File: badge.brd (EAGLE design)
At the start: 53.8 x 85.3 mm, 33 parts, among them IC1 MCP1703CB, U1 ESP8266, U2 AT25SF041-SOIC8, Y1 26MHz

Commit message: for ys
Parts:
- removed D2: 1N4148, adafruit:SOD-323F
- removed E1: ANTENNATRACE, SparkFun-RF:TRACE_ANTENNA_2.4GHZ_25.7MM
- removed IC1: MCP1703CB, linear:SOT23
- removed JP2: (no value), pinhead:1X05
- removed JP3: (no value), pinhead:1X04
- removed S1, S2, S3, S4, S5: (no value), gm2:TACT-SW-4P-SMD
- removed Y1: 26MHz, SparkFun-FreqCtrl:CRYSTAL-SMD-5X3
- added ANT1: AN9520, badge:AN9520
- added D3: 1N4148, adafruit:SOD-323F
- added SW1: MK12C02, badge:MK12C02
- added U$1, U$2, U$3, U$4, U$5, U$6: TOUCHSWITCH, badge:EVQQWN03W
- added U3: LM317EMP-SOT223, Seeed-OPL-ic:SOT-223
- added XTAL1: 26MHZ, badge:XRCGB_F_P
- C1, C2, C3, C4, C5, C6, C7, C8, C9: device rcl:C0805 -> resistor:C0603K
- R1, R2, R3, R4, R5, R6: device rcl:R0805 -> resistor:R0603W
- moved C3 64.4 mm to (74.9, 26.4), turned to 0 degrees
- moved C2 58.7 mm to (80.2, 37.9), turned to 90 degrees
- moved R1 55.9 mm to (82.4, 37.1)
- moved R2 55.1 mm to (72.7, 40.2), turned to 0 degrees
- moved U1 52.0 mm to (74.9, 35.6)
- moved C6 50.6 mm to (82.4, 34.3), turned to 180 degrees
- moved R6 50.3 mm to (68.3, 31.4), turned to 270 degrees
- moved U2 49.7 mm to (74.9, 29.7), turned to 90 degrees
- moved C8 48.8 mm to (79.1, 41.1), turned to 270 degrees
- moved D1 48.3 mm to (70.0, 31.4), turned to 270 degrees
- moved R4 45.9 mm to (77.8, 41.1), turned to 90 degrees
- moved C7 44.3 mm to (82.4, 35.7)
- moved JP1 42.0 mm to (87.6, 33.5), turned to 90 degrees
- moved C1 41.9 mm to (74.9, 41.1)
- moved C4 35.6 mm to (22.2, 40.8), turned to 180 degrees
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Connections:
- removed net GPIO2: JP3.2, S1.1, S1.2, U1.14
- removed net N$7: C7.1, U1.28, Y1.1
- removed net SPI_CLK: JP2.4, LCD1.2, U1.9
- removed net SPI_CS: JP2.5, S4.1, S4.2, U1.13
- removed net SPI_SI: JP2.3, LCD1.3, U1.12
- removed net SPI_SO: JP2.2, LCD1.4, U1.10
- new net ANT: ANT1.P$1, U1.2
- new net GPIO12/SPI_SO: LCD1.4, U1.10
- new net GPIO13/SPI_SI: LCD1.3, U1.12
- new net GPIO14/SPI_CLK/SCL: LCD1.2, U1.9
- new net GPIO15/SPI_CS: U$3.P$2, U$3.P$3, U$4.P$2, U$4.P$3, U1.13
- new net GPIO16: U1.8
- new net GPIO2/SDA: U$1.P$1, U$1.P$4, U$3.P$1, U$3.P$4, U$5.P$1, U$5.P$4, U1.14
- net 5V: now also D3.A
- net ADC: no longer JP2.1
- net GND: now also C6.1, C7.1, U3.1; no longer C6.2, C7.2, E1.GND, E1.GND2, IC1.1, S1.3, S1.4, S2.3, S2.4, S3.3, S3.4, S4.3, S4.4, S5.3, S5.4
- net GPIO0: now also U$5.P$2, U$5.P$3, U$6.P$2, U$6.P$3; no longer JP3.1, S5.1, S5.2
- net GPIO4: now also U$2.P$1, U$2.P$4, U$4.P$1, U$4.P$4, U$6.P$1, U$6.P$4; no longer JP3.3, S2.1, S2.2
- net GPIO5: now also U$1.P$2, U$1.P$3, U$2.P$2, U$2.P$3; no longer JP3.4, S3.1, S3.2
- net N$1: now also SW1.P$2, U3.3; no longer E1.ANT, U1.2
- net N$5: now also D3.C, SW1.P$1; no longer IC1.3
- net N$6: now also C6.2, U1.27, XTAL1.P$2; no longer D2.C, U1.8
- net N$8: now also C7.2, U1.28, XTAL1.P$4; no longer C6.1, U1.27, Y1.3
- net RESET: no longer D2.A
- net VCC: now also U3.2, U3.TER; no longer IC1.2
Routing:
- net GND: track 60.7 -> 0.00 mm
- net GPIO4: track 0.00 -> 20.4 mm
- net GPIO2/SDA: track 0.00 -> 20.4 mm
- net GPIO15/SPI_CS: track 0.00 -> 13.6 mm
- net ANT: track 0.00 -> 7.69 mm
- net GPIO5: track 0.00 -> 7.41 mm
- net GPIO0: track 9.10 -> 13.6 mm
- removed copper zone on layer 1, net GND
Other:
- board size 53.8 x 85.3 mm -> 90 x 50 mm

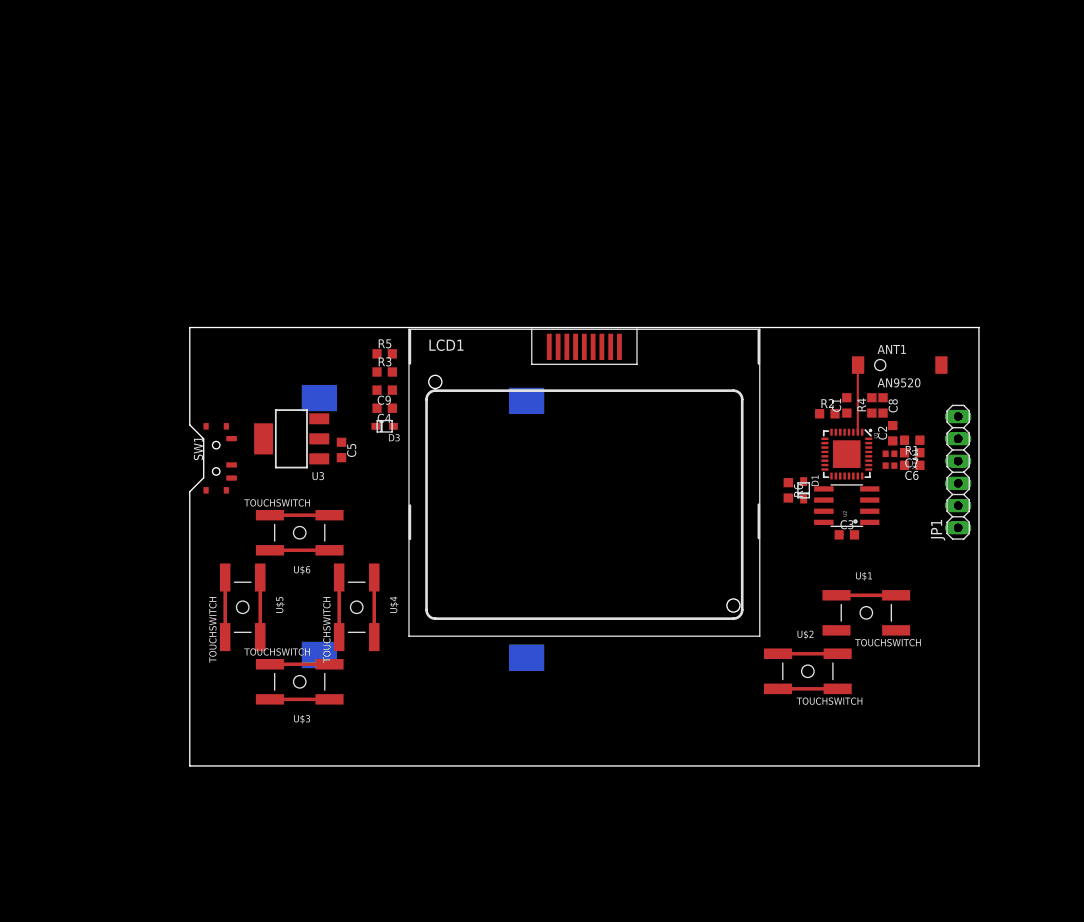
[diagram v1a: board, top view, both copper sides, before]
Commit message: switching over to ESP-12e/f
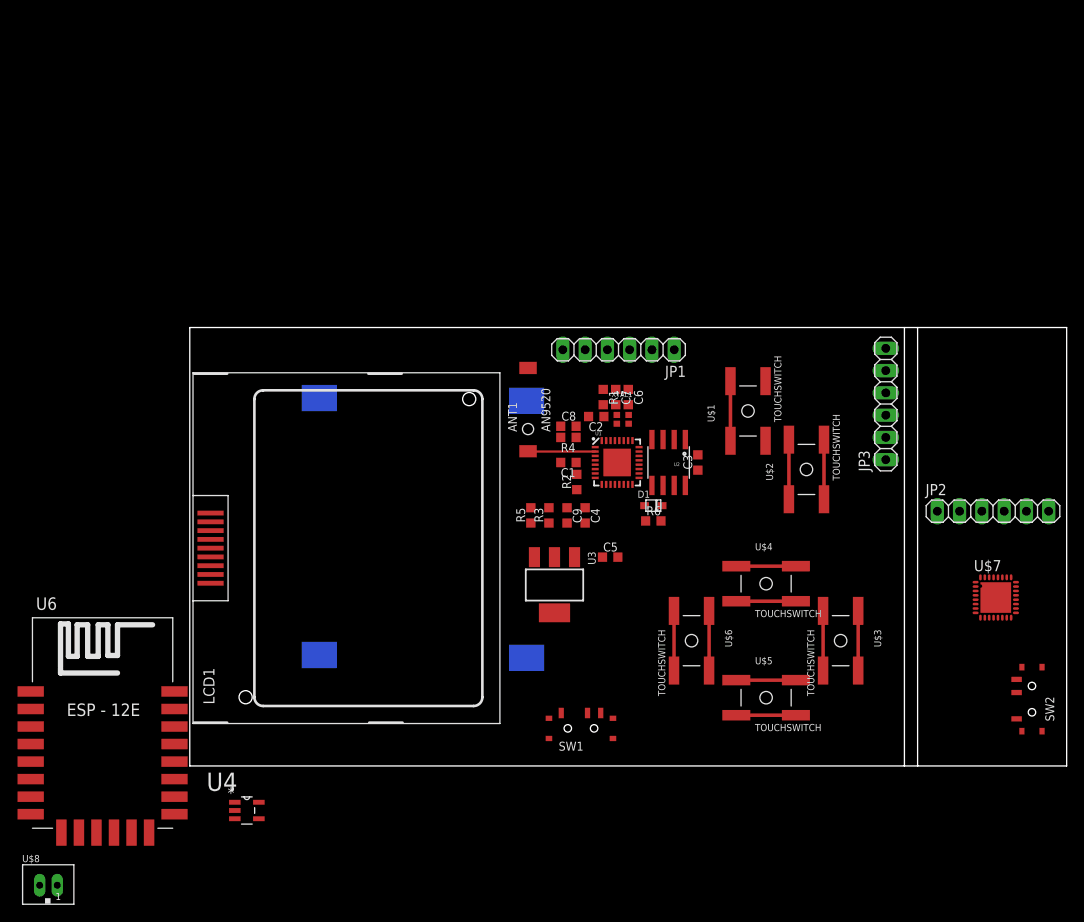
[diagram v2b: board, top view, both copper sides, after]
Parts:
- removed D3: 1N4148, adafruit:SOD-323F
- added JP2, JP3: (no value), pinhead:1X06
- added SW2: MK12C02, badge:MK12C02
- added U$7: CY7C65213-32LTXI, cypress_usb-serial:QFN32
- added U$8: JST-PH_2-PIN_HEADER, SRG:JST_B2B-PH_HEADER
- added U4: MCP73832T-2DCI/OT, Microchip_By_element14_Batch_1:SOT95P300X145-5N
- added U6: (no value), esp8266modules:ESP12E-SMD
- moved U$3 61.9 mm to (74.2, 14.3), turned to 180 degrees
- moved U$5 60.6 mm to (65.7, 7.79), turned to 270 degrees
- moved SW1 51.8 mm to (44.6, 4.29), turned to 0 degrees
- moved U$4 46.8 mm to (65.7, 20.8), turned to 270 degrees
- moved U$6 46.3 mm to (57.2, 14.3), turned to 180 degrees
- moved ANT1 42.7 mm to (38.6, 40.6), turned to 90 degrees
- moved JP1 41.2 mm to (48.9, 47.5), turned to 180 degrees
- moved C8 36.0 mm to (43.2, 38.7), turned to 0 degrees
- moved R1 35.6 mm to (47.1, 42.1), turned to 270 degrees
- moved R4 34.8 mm to (43.2, 37.5), turned to 180 degrees
- moved C7 34.4 mm to (48.6, 42.1), turned to 270 degrees
- moved U3 34.3 mm to (41.6, 20.6), turned to 180 degrees
- moved C2 33.9 mm to (46.4, 39.8), turned to 180 degrees
- moved C6 33.3 mm to (50.0, 42.1), turned to 270 degrees
- moved C5 33.0 mm to (47.9, 23.8), turned to 0 degrees
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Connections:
- new net AGND: U$7.24
- new net N$10: JP2.2, JP3.2
- new net N$11: JP2.3, JP3.3
- new net N$12: JP2.4, JP3.4
- new net N$13: JP2.5, JP3.5
- new net N$14: JP2.6, JP3.6
- new net N$7: JP2.1, JP3.1
- new net VCCD: U$7.16
- new net VCCIO: U$7.1
- new net VDD: U4.4
- net 5V: now also SW1.P$3; no longer D3.A
- net GND: now also U$7.17, U$7.20, U$7.4
- net N$1: now also C4.1, SW1.P$1; no longer SW1.P$2
- net N$5: now also SW1.P$2; no longer C4.1, D3.C, SW1.P$1
- net VCC: now also U$7.19
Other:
- board size 90 x 50 mm -> 100 x 50 mm

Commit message: before the big change
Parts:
- removed ANT1: AN9520, badge:AN9520
- removed B1, B2: BATTERY, gm2:BATT-HOLDER-20MM
- removed D1: 1N4148, adafruit:SOD-323F
- removed JP1, JP2, JP3: (no value), pinhead:1X06
- removed SW2: MK12C02, badge:MK12C02
- removed U$6: TOUCHSWITCH, badge:EVQQWN03W
- removed U$8: JST-PH_2-PIN_HEADER, SRG:JST_B2B-PH_HEADER
- removed U1: ESP8266, SparkFun-RF:QFN32
- removed U2: AT25SF041-SOIC8, SparkFun-RF:SO08
- removed U3: LM317EMP-SOT223, Seeed-OPL-ic:SOT-223
- removed XTAL1: 26MHZ, badge:XRCGB_F_P
- added C10, C12: 0.1uF, resistor:C0603K
- added C11: 4.7uF, resistor:C0603K
- added CON1: PH_2, badge:PH_2
- added J1, J2: (no value), SparkFun-Connectors:1X03
- added J10: (no value), SparkFun-Connectors:1X14
- added J3, J4: (no value), SparkFun-Connectors:1X06
- added J5, J6, J8: (no value), SparkFun-Connectors:1X10
- added LED1, LED2, LED3: (no value), led:SML0805
- added R10, R7, R8, R9: 470, resistor:R0603W
- added R11: 590k, resistor:R0603W
- added R12: 280k, resistor:R0603W
- added R13: 82k, resistor:R0603W
- added R14, R15: 1k, resistor:R0603W
- added SJ1, SJ2, SJ3, SJ4: SOLDERJUMPERTRACE, SparkFun-Retired:SJ_2S-TRACE
- added U$10: USBMICRO, badge:USBMICRO
- added U$11: MCP1824T-ADJE/OT, Microchip_By_element14_Batch_1:SOT95P270X145-5N
- added U$9: MCP1824T-3302E/OT, Microchip_By_element14_Batch_1:SOT95P270X145-5N
- C1: value 10uF -> 4.7uF
- C2, C3: value 0.1uF -> 4.7uF
- C4: value 1uF -> 1uF/X7R
- C5: value 10uF -> 1uF/X7R
- C6: value 12pF -> 1uF
- C7: value 12pF -> 1uF/X7R
- C8: value 1uF -> 4.7uF
- R1: value 12k -> 100k
- R2: value 12K -> 470
- R4: value 12K -> 100k
- R6: value 12K -> 2k
- moved U6 72.2 mm to (54.6, 35.2), turned to 90 degrees
- moved R1 56.3 mm to (92.0, 8.10), turned to 0 degrees
- moved C6 50.2 mm to (91.4, 13.7), turned to 180 degrees
- moved C7 49.8 mm to (93.0, 19.7), turned to 90 degrees
- moved C8 47.0 mm to (89.9, 33.5)
- moved C9 44.3 mm to (3.41, 8.65), turned to 90 degrees
- moved U4 43.5 mm to (45.9, 13.4), turned to 90 degrees
- moved C3 40.6 mm to (90.9, 11.0)
- moved R3 39.8 mm to (3.41, 15.5)
- moved R5 39.1 mm to (3.41, 12.1), turned to 270 degrees
- moved C2 31.6 mm to (49.5, 8.41)
- moved U$5 30.4 mm to (73.7, 37.1), turned to 180 degrees
- moved U$1 27.8 mm to (54.5, 14.3)
- moved C1 24.5 mm to (43.3, 10.1), turned to 90 degrees
- moved R2 22.4 mm to (41.8, 10.1)
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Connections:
- removed net AGND: U$7.24
- removed net ANT: ANT1.P$1, U1.2
- removed net N$13: JP2.5, JP3.5
- removed net N$14: JP2.6, JP3.6
- removed net N$15: JP1.5
- removed net N$2: R1.2, U1.31
- removed net N$5: B1.+, SW1.P$2
- removed net N$8: C7.2, U1.28, XTAL1.P$4
- removed net SD_CLK: U1.21, U2.6
- removed net SD_CS0: U1.20, U2.1
- removed net SD_HD: U1.18, U2.7
- removed net SD_SI: U1.23, U2.5
- removed net SD_SO: U1.22, U2.2
- removed net SD_WP: U1.19, U2.3
- removed net U0RX: JP1.3, U1.25
- removed net U0TX: JP1.2, U1.26
- removed net VCCD: U$7.16
- removed net VCCIO: U$7.1
- removed net VDD: U4.4
- new net BATT+: C1.1, CON1.P$2, SW1.P$3, U4.3
- new net CH_PD: J8.6, SJ1.2, U6.CH_PD
- new net CS0: J10.1, U6.CS0
- new net CTS: J5.8, U$7.8
- new net D+: U$10.P$D+, U$7.14
- new net D-: U$10.P$D-, U$7.15
- new net DCD: J5.4, U$7.7
- new net DSR: J5.5, U$7.6
- new net GPIO10: J10.5, U6.GPIO10
- new net GPIO9: J10.6, U6.GPIO9
- new net ID: U$10.P$ID
- new net MISO: J10.2, U6.MISO
- new net MOSI: J10.3, U6.MOSI
- new net N$16: J1.1, R11.2
- new net N$17: J1.3, R12.2
- new net N$18: R10.2, R9.1, U$7.18
- new net N$19: C6.1, J1.2, J2.1, U$11.5
- new net N$20: C7.2, U$7.16
- new net N$28: R14.1, SJ3.2
- new net N$30: R15.1, SJ4.2
- new net RI: J5.3, U$7.3
- new net RTS: J3.5, J4.5, J5.7, SJ2.1, U$7.32
- new net RX: J10.13, J3.3, J4.3, J5.10, U$7.30, U6.RXD0
- new net SCLK: J10.4, U6.SCLK
- new net TX: J10.14, J3.2, J4.2, J5.9, U$7.2, U6.TXD0
- new net USB_GPIO0: J6.3, U$7.22
- new net USB_GPIO1: J6.4, U$7.21
- new net USB_GPIO2: J6.5, U$7.10
- new net USB_GPIO3: J6.6, U$7.11
- new net USB_GPIO4: J6.7, U$7.9
- new net USB_GPIO5: J6.8, U$7.5
- new net USB_GPIO6: J6.9, U$7.12
- new net USB_GPIO7: J6.10, U$7.13
- new net VADJ: R11.1, R12.1, R13.2, U$11.4
- new net V_IO: C11.2, C12.2, J2.2, J6.1, U$7.1
- net 5V: now also C10.2, C2.1, C3.2, C8.2, J2.3, J3.4, J4.4, J5.1, LED1.A, LED3.A, R9.2, SW1.P$2, U$10.P$VCC, U$11.1, U$7.19, U4.4; no longer JP1.4, SW1.P$3
- net ADC: now also J8.7, U6.ADC; no longer U1.6
- net DTR: now also J3.1, J4.1, J5.6, SJ1.1, U$7.31; no longer C8.1, D1.C, JP1.1
- net GND: now also C10.1, C11.1, C12.1, C3.1, C6.2, C8.1, CON1.P$1, J10.11, J10.12, J3.6, J4.6, J5.2, J6.2, J8.8, R10.1, R13.1, R14.2, R4.1, R6.1, R7.1, R8.1, U$10.P$GND, U$11.2, U$7.24, U$9.2, U4.2, U6.GND; no longer B2.-, C3.2, C6.1, JP1.6, U1.EP, U2.4, U3.1
- net GPIO0: now also J10.10, SJ4.1, U6.GPIO0; no longer D1.A, R6.1, U$5.P$2, U$5.P$3, U$6.P$2, U$6.P$3, U1.15
- net GPIO12/SPI_SO: now also J8.5, U6.GPIO12; no longer U1.10
- net GPIO13/SPI_SI: now also J8.4, U6.GPIO13; no longer U1.12
- net GPIO14/SPI_CLK/SCL: now also J8.3, U6.GPIO14; no longer U1.9
- net GPIO15/SPI_CS: now also J8.2, SJ3.1, U6.GPIO15; no longer U$3.P$2, U$3.P$3, U$4.P$2, U$4.P$3, U1.13
- net GPIO16: now also J8.1, U6.GPIO16; no longer U1.8
- net GPIO2/SDA: now also J10.9, U6.GPIO2; no longer U$1.P$1, U$1.P$4, U$3.P$1, U$3.P$4, U$5.P$1, U$5.P$4, U1.14
- net GPIO4: now also J10.8, U6.GPIO4; no longer U$2.P$1, U$2.P$4, U$4.P$1, U$4.P$4, U$6.P$1, U$6.P$4, U1.16
- net GPIO5: now also J10.7, U6.GPIO5; no longer U$1.P$2, U$1.P$3, U$2.P$2, U$2.P$3, U1.24
- net N$1: now also U$9.1; no longer U3.3
- net N$10: now also R2.1, U4.1; no longer JP2.2, JP3.2
- net N$11: now also R1.2, U$11.3; no longer JP2.3, JP3.3
- net N$12: now also LED3.C, R8.2; no longer JP2.4, JP3.4
- net N$4: now also R4.2, U$9.3; no longer R2.1, U1.7
- net N$6: now also R6.2, U4.5; no longer C6.2, U1.27, XTAL1.P$2
- net N$7: now also LED2.C, R7.2; no longer JP2.1, JP3.1
- net N$9: now also LED1.C, R2.2; no longer B1.-, B2.+
- net RESET: now also SJ2.2, U6.RESET; no longer C8.2, R4.1, U1.32
- net VCC: now also J8.10, J8.9, LED2.A, R15.2, U$9.5, U6.VCC; no longer C1.1, C2.1, C3.1, R2.2, R4.2, R6.2, U$7.19, U1.1, U1.11, U1.17, U1.29, U1.3, U1.30, U1.4, U2.8, U3.2, U3.TER
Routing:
- net GND: track 0.00 -> 227.7 mm, vias 0 -> 8
- net 5V: track 0.00 -> 182.0 mm, vias 0 -> 4
- net VCC: track 0.00 -> 112.0 mm, vias 0 -> 2
- net GPIO12/SPI_SO: track 0.00 -> 104.7 mm, vias 0 -> 3
- net GPIO13/SPI_SI: track 0.00 -> 104.5 mm, vias 0 -> 3
- net GPIO14/SPI_CLK/SCL: track 0.00 -> 104.4 mm, vias 0 -> 1
- net RX: track 0.00 -> 62.7 mm, vias 0 -> 2
- net TX: track 0.00 -> 57.2 mm
- net ADC: track 0.00 -> 55.7 mm, vias 0 -> 1
- net CH_PD: track 0.00 -> 53.5 mm, vias 0 -> 1
- net GPIO16: track 0.00 -> 51.9 mm, vias 0 -> 2
- net GPIO15/SPI_CS: track 13.6 -> 56.6 mm, vias 0 -> 1
- net RTS: track 0.00 -> 30.6 mm
- net DTR: track 0.00 -> 29.4 mm, vias 0 -> 1
- net CS0: track 0.00 -> 24.7 mm, vias 0 -> 1
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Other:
- outline, holes or cut-outs redrawn
- board text added: "Init:6.25mil"

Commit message: the change cometh
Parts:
- removed C10, C12: 0.1uF, resistor:C0603K
- removed C11, C8: 4.7uF, resistor:C0603K
- removed C6: 1uF, resistor:C0603K
- removed C7: 1uF/X7R, resistor:C0603K
- removed J4: (no value), SparkFun-Connectors:1X06
- removed J5, J6: (no value), SparkFun-Connectors:1X10
- removed U$11: MCP1824T-ADJE/OT, Microchip_By_element14_Batch_1:SOT95P270X145-5N
- removed U$7: CY7C65213-32LTXI, cypress_usb-serial:QFN32
- added IC1: CP2102, silabs:MLP28
- added LED4, LED5, LED6, LED7, LED8: (no value), led:SML0805
- added R16, R17: 1k, resistor:R0603W
- added SJ5: SOLDERJUMPERTRACE, SparkFun-Retired:SJ_2S-TRACE
- J2: device SparkFun-Connectors:1X03 -> SparkFun-Connectors:1X08
- J3: value (none) -> 2X6 FEMALE; device SparkFun-Connectors:1X06 -> SparkFun-Connectors:2X6
- R1: value 100k -> 470
- R11: value 590k -> 470
- R12: value 280k -> 470
- R13: value 82k -> 1k
- moved R13 96.7 mm to (-1.43, -4.92), turned to 0 degrees
- moved R11 78.1 mm to (24.8, 46.4)
- moved R10 74.2 mm to (19.8, 46.4), turned to 180 degrees
- moved R1 72.3 mm to (19.8, 3.89), turned to 180 degrees
- moved SJ2 70.0 mm to (-4.37, -4.84)
- moved R12 69.8 mm to (32.9, 46.4), turned to 180 degrees
- moved SJ1 67.7 mm to (-1.43, -0.71)
- moved R9 66.4 mm to (32.9, 3.89)
- moved LED3 63.3 mm to (20.0, 6.19)
- moved R8 58.3 mm to (24.8, 3.89)
- moved J1 50.2 mm to (51.5, 25.1), turned to 180 degrees
- moved J3 50.1 mm to (47.5, 32.7), turned to 90 degrees
- moved U$10 43.3 mm to (47.1, 1.43)
- moved J2 38.8 mm to (43.9, 7.30)
- moved C3 37.7 mm to (53.2, 9.84), turned to 270 degrees
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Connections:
- removed net CTS: J5.8, U$7.8
- removed net DCD: J5.4, U$7.7
- removed net DSR: J5.5, U$7.6
- removed net DTR: J3.1, J4.1, J5.6, SJ1.1, U$7.31
- removed net N$11: R1.2, U$11.3
- removed net N$12: LED3.C, R8.2
- removed net RI: J5.3, U$7.3
- removed net RTS: J3.5, J4.5, J5.7, SJ2.1, U$7.32
- removed net USB_GPIO0: J6.3, U$7.22
- removed net USB_GPIO1: J6.4, U$7.21
- removed net USB_GPIO2: J6.5, U$7.10
- removed net USB_GPIO3: J6.6, U$7.11
- removed net USB_GPIO4: J6.7, U$7.9
- removed net USB_GPIO5: J6.8, U$7.5
- removed net USB_GPIO6: J6.9, U$7.12
- removed net USB_GPIO7: J6.10, U$7.13
- removed net VADJ: R11.1, R12.1, R13.2, U$11.4
- removed net V_IO: C11.2, C12.2, J2.2, J6.1, U$7.1
- new net N$15: R17.1, SJ5.2
- new net N$21: LED4.C, R8.2
- new net N$22: LED5.C, R9.2
- new net N$23: LED6.C, R10.2
- new net N$24: LED7.C, R11.2
- new net N$25: LED8.C, R12.2
- new net N$5: R13.1, SJ1.2
- new net N$8: R16.1, SJ2.2
- new net S_CTS: IC1.23, J2.8
- new net S_DCD: IC1.1, J2.2
- new net S_DSR: IC1.27, J2.4
- new net S_DTR: IC1.28, J2.3, J3.2
- new net S_RI: IC1.2, J2.1
- new net S_RTS: IC1.24, J2.7, J3.10
- new net S_RXD: IC1.25, J2.6, J3.4
- new net S_TXD: IC1.26, J2.5, J3.6
- net 5V: now also IC1.7, IC1.8, J3.7, J3.8; no longer C10.2, C3.2, C8.2, J2.3, J3.4, J4.4, J5.1, LED3.A, R9.2, U$11.1, U$7.19
- net CH_PD: now also J3.1, SJ5.1; no longer SJ1.2
- net D+: now also IC1.4; no longer U$7.14
- net D-: now also IC1.5; no longer U$7.15
- net GND: now also C3.2, IC1.3, IC1.EXP, IC1.M, J3.11, J3.12, R11.1, R12.1, R9.1; no longer C10.1, C11.1, C12.1, C3.1, C6.2, C7.1, C8.1, J3.6, J4.6, J5.2, J6.2, R13.1, U$11.2, U$7.17, U$7.20, U$7.24, U$7.4
- net GPIO2/SDA: now also SJ1.1
- net N$16: now also IC1.11, J1.2; no longer J1.1, R11.2
- net N$17: now also IC1.12; no longer R12.2
- net N$18: now also LED3.C, R1.2; no longer R10.2, R9.1, U$7.18
- net N$19: now also IC1.9, J1.1; no longer C6.1, J1.2, J2.1, U$11.5
- net N$20: now also C3.1, IC1.6; no longer C7.2, U$7.16
- net RESET: now also J3.9, SJ2.1; no longer SJ2.2
- net RX: now also J3.5; no longer J3.3, J4.3, J5.10, U$7.30
- net TX: now also J3.3; no longer J3.2, J4.2, J5.9, U$7.2
- net VCC: now also LED3.A, LED4.A, LED5.A, LED6.A, LED7.A, LED8.A, R13.2, R16.2, R17.2
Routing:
- net 5V: track 182.0 -> 105.6 mm
- net VCC: track 112.0 -> 182.9 mm, vias 2 -> 4
- net RX: track 62.7 -> 15.9 mm
- net TX: track 57.2 -> 13.9 mm
- net S_RTS: track 0.00 -> 39.4 mm, vias 0 -> 1
- net S_DTR: track 0.00 -> 36.6 mm, vias 0 -> 1
- net S_TXD: track 0.00 -> 34.0 mm
- net RTS: track 30.6 -> 0.00 mm
- net DTR: track 29.4 -> 0.00 mm, vias 1 -> 0
- net S_RXD: track 0.00 -> 28.6 mm
- net GPIO12/SPI_SO: track 104.7 -> 123.6 mm
- net GPIO13/SPI_SI: track 104.5 -> 123.5 mm
- net GPIO14/SPI_CLK/SCL: track 104.4 -> 123.2 mm
- net N$17: track 0.00 -> 16.2 mm
- net N$16: track 0.00 -> 15.7 mm
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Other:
- outline, holes or cut-outs redrawn

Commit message: before addition of autoreset
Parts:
- removed R1, R10, R11, R12, R8, R9: 470, resistor:R0603W
- removed R13, R15, R16, R17: 1k, resistor:R0603W
- removed SJ2, SJ4, SJ5: SOLDERJUMPERTRACE, SparkFun-Retired:SJ_2S-TRACE
- added SW2: MK12C02, badge:MK12C02
- added U$11, U$6, U$7, U$8: RES_ARR, Simplex-rlc:YC164
- added U1, U2: SMBT2222A, badge:SOT95P290X110-3N
- C1, C2, C3: value 4.7uF -> 10uF
- C4, C5: value 1uF/X7R -> 10uF
- LED1: value (none) -> RED
- LED2: value (none) -> YELLOW
- R2, R7: value 470 -> 220
- moved SJ1 67.1 mm to (56.8, 32.8), turned to 270 degrees
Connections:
- removed net N$21: LED4.C, R8.2
- removed net N$25: LED8.C, R12.2
- removed net N$30: R15.1, SJ4.2
- removed net N$8: R16.1, SJ2.2
- new net N$11: LED3.C, U$6.8
- new net N$12: LED4.C, U$6.7
- new net N$13: LED5.C, U$6.6
- new net N$2: LED3.A, LED4.A, LED5.A, LED6.A, LED7.A, LED8.A, SW2.P$1
- net CH_PD: now also U$11.6; no longer SJ5.1
- net GND: now also U$6.1, U$6.2, U$6.3, U$7.1, U$7.2, U$7.3; no longer R1.1, R10.1, R11.1, R12.1, R8.1, R9.1
- net GPIO0: now also U$11.8, U1.3; no longer SJ4.1
- net GPIO2/SDA: now also U$11.7; no longer SJ1.1
- net N$15: now also U$8.4, U1.1; no longer R17.1, SJ5.2
- net N$18: now also U$8.3, U2.1; no longer LED3.C, R1.2
- net N$22: now also LED6.C, U$7.6; no longer LED5.C, R9.2
- net N$23: now also LED7.C, U$7.7; no longer LED6.C, R10.2
- net N$24: now also LED8.C, U$7.8; no longer LED7.C, R11.2
- net N$5: now also SJ1.1, U$11.1, U$11.2, U$11.3, U$11.4; no longer R13.1, SJ1.2
- net RESET: now also U$11.5, U2.3; no longer SJ2.1
- net S_DTR: now also U$8.6, U1.2
- net S_RTS: now also U$8.5, U2.2
- net VCC: now also SJ1.2, SW2.P$3; no longer LED3.A, LED4.A, LED5.A, LED6.A, LED7.A, LED8.A, R13.2, R15.2, R16.2, R17.2
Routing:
- net VCC: track 182.9 -> 106.2 mm, vias 4 -> 3
- net GND: track 229.5 -> 163.0 mm
- net N$25: track 2.39 -> 0.00 mm
- net N$24: track 2.39 -> 0.00 mm
- net N$23: track 2.39 -> 0.00 mm
- net N$22: track 2.31 -> 0.00 mm
- net N$21: track 2.31 -> 0.00 mm
- net N$18: track 2.31 -> 0.00 mm
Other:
- outline, holes or cut-outs redrawn
